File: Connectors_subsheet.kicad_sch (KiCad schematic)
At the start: 34 parts, among them J3 SDOAG_Connector, J4 Power_Connector, J5 Ultrasonic, J6 USB_A, J7 IMU_1, J8 IMU_2, Q1 BSS138

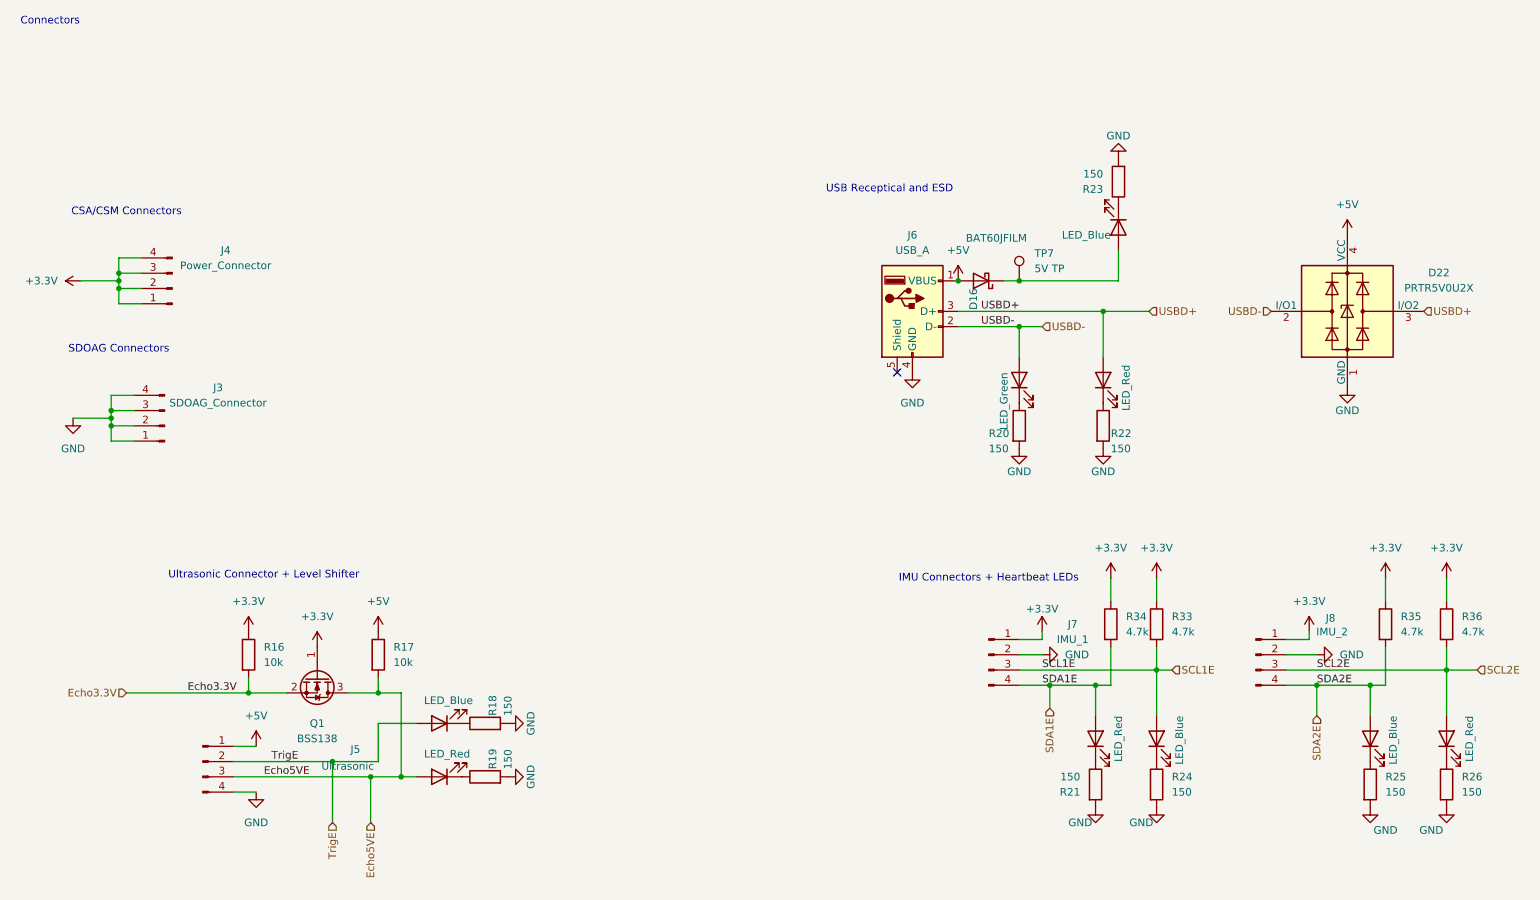
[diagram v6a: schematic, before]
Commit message: removed LEDs on IMU and ultrasonic
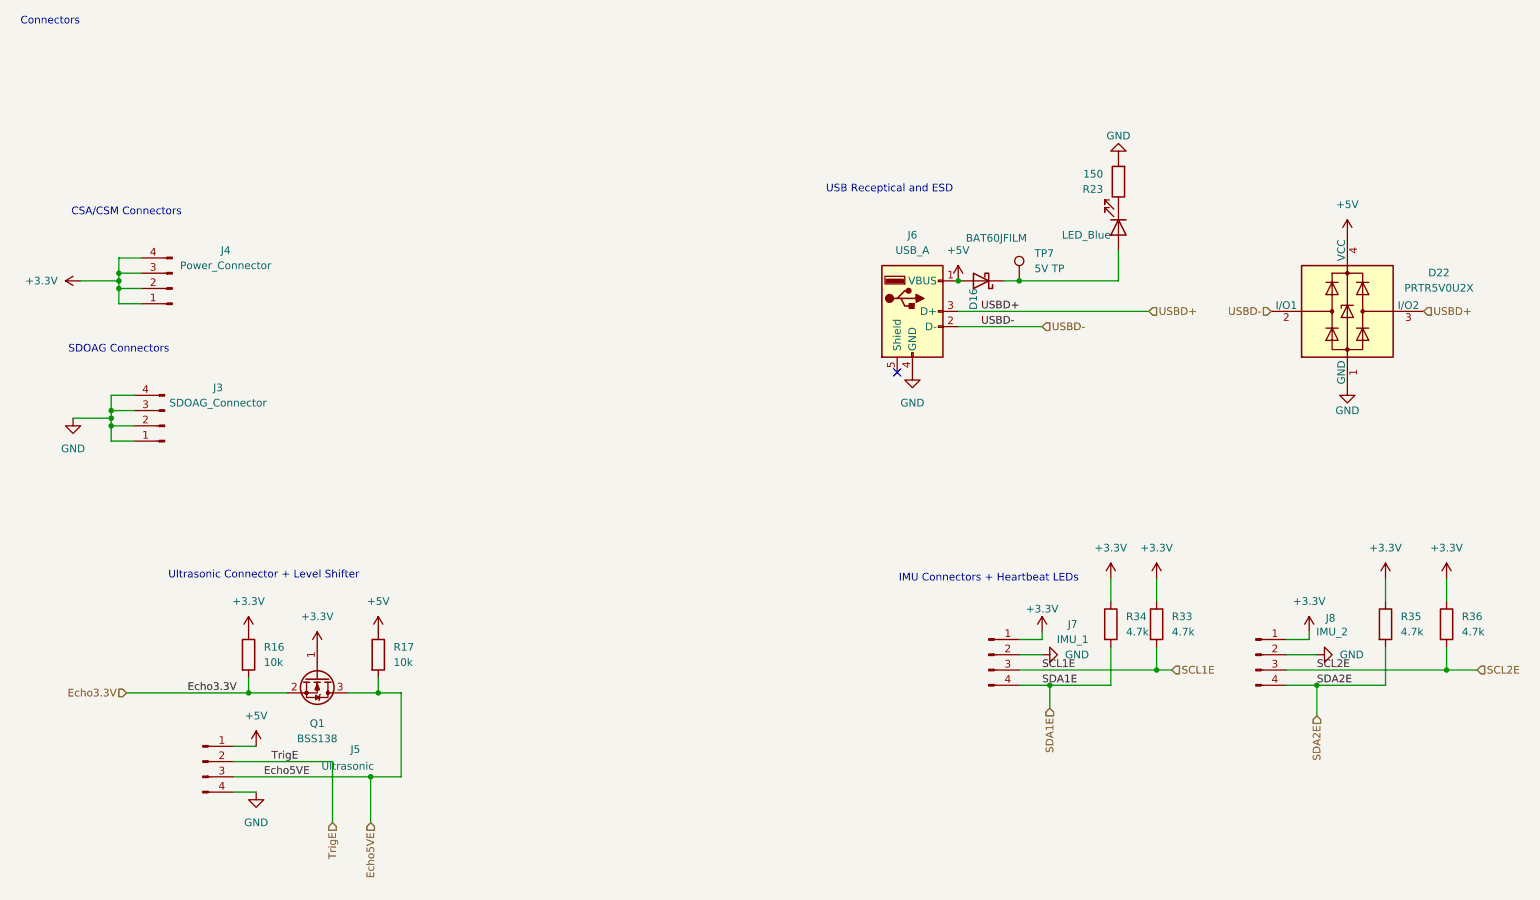
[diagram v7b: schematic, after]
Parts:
- removed D14, D21, D23: LED_Blue, LED_SMD:LED_0805_2012Metric_Pad1.15x1.40mm_HandSolder, symbol Device:LED
- removed D15, D18, D19, D24: LED_Red, LED_SMD:LED_0805_2012Metric_Pad1.15x1.40mm_HandSolder, symbol Device:LED
- removed D17: LED_Green, LED_SMD:LED_0805_2012Metric_Pad1.15x1.40mm_HandSolder, symbol Device:LED
- removed R18, R19, R20, R21, R22, R24, R25, R26: 150, Resistor_SMD:R_0805_2012Metric_Pad1.20x1.40mm_HandSolder, symbol Device:R

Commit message: updated fp
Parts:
- removed TP7: 5V TP, TestPoint:TestPoint_Loop_D3.50mm_Drill1.4mm_Beaded, symbol Connector:TestPoint
- D16: footprint Diode_SMD:D_0805_2012Metric_Pad1.15x1.40mm_HandSolder -> Diode_SMD:D_SOD-323_HandSoldering
- D22: footprint Package_TO_SOT_SMD:SOT-143 -> Library:PRT
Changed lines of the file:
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@@
-	)
-	(junction
-		(at 190.5 66.04)
-		(diameter 0)
-		(color 0 0 0 0)
 	)
 	(junction
@@
 	(wire
 		(pts
-			(xy 190.5 66.04) (xy 207.01 66.04)
-		)
-		(stroke
-			(width 0)
-			(type default)
-		)
-	)
-	(wire
-		(pts
 			(xy 195.58 133.35) (xy 205.74 133.35)
 		)
@@
 	(wire
 		(pts
-			(xy 187.96 66.04) (xy 190.5 66.04)
+			(xy 187.96 66.04) (xy 207.01 66.04)
 		)
 		(stroke
@@
 	)
 	(symbol
-		(lib_id "Connector:TestPoint")
-		(at 190.5 66.04 0)
-		(unit 1)
-		(exclude_from_sim no)
-		(in_bom yes)
-		(on_board yes)
-		(dnp no)
-		(fields_autoplaced yes)
-		(property "Reference" "TP7"
-			(at 193.04 61.4679 0)
-			(effects
-				(font
-					(size 1.27 1.27)
-				)
-				(justify left)
-			)
-		)
-		(property "Value" "5V TP"
-			(at 193.04 64.0079 0)
-			(effects
-				(font
-					(size 1.27 1.27)
-				)
-				(justify left)
-			)
-		)
-		(property "Footprint" "TestPoint:TestPoint_Loop_D3.50mm_Drill1.4mm_Beaded"
-			(at 195.58 66.04 0)
-			(effects
-				(font
-					(size 1.27 1.27)
-				)
-				(hide yes)
-			)
-		)
-		(property "Datasheet" "~"
-			(at 195.58 66.04 0)
-			(effects
-				(font
-					(size 1.27 1.27)
-				)
-				(hide yes)
-			)
-		)
-		(property "Description" "test point"
-			(at 190.5 66.04 0)
-			(effects
-				(font
-					(size 1.27 1.27)
-				)
-				(hide yes)
-			)
-		)
-		(pin "1"
-		)
-		(instances
-			(project "PCB_Schematic"
-				(path "/a0c17764-e0d1-4df5-b871-1489cf266494/ca0ff4d7-ae36-445b-939c-5f82f56efbb4"
-					(reference "TP7")
-					(unit 1)
-				)
-			)
-		)
-	)
-	(symbol
 		(lib_name "BSS138_1")
 		(lib_id "Transistor_FET:BSS138")
@@
 			)
 		)
-		(property "Footprint" "Diode_SMD:D_0805_2012Metric_Pad1.15x1.40mm_HandSolder"
+		(property "Footprint" "Diode_SMD:D_SOD-323_HandSoldering"
 			(at 184.15 66.04 0)
 			(effects
@@
 			)
 		)
-		(property "Footprint" "Package_TO_SOT_SMD:SOT-143"
+		(property "Footprint" "Library:PRT"
 			(at 246.634 71.12 0)
 			(effects
